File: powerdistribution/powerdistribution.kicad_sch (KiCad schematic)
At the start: 110 parts, among them IC1 STEF01FTR, IC2 STEF01FTR, IC3 STEF01FTR, J1 282837-2, J2 282837-2, J3 M20-6102045, J4 Screw_Terminal_01x02, J5 Screw_Terminal_01x02, Q1 IRLML0030, Q2 IRLML0030, Q3 MMBT3904, Q4 SI4925DDY-T1-GE3, SW1 RA1H1C112R, SW2 RA1H1C112R, U1 BQ7790512PW, U2 AP64501QSP-13, U3 AP64501QSP-13, U4 AP64501QSP-13

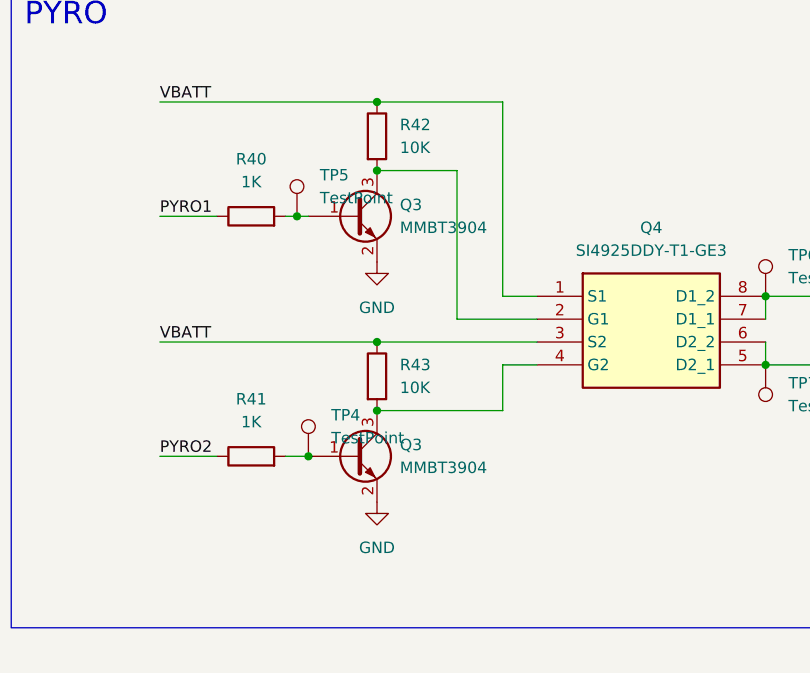
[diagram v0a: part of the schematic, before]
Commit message: swapped pyro transistors for same ones on bms
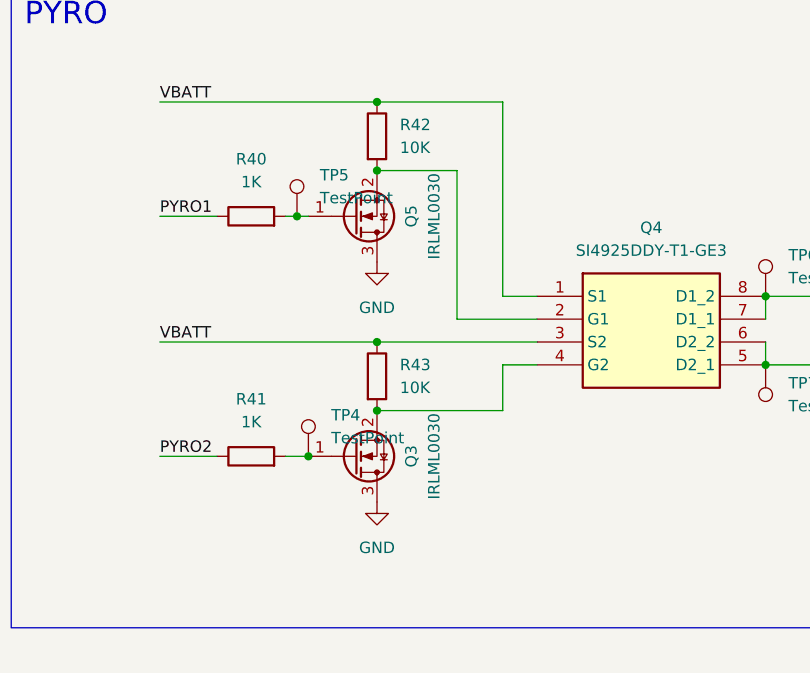
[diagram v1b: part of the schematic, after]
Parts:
- removed Q3 (x2): MMBT3904, Package_TO_SOT_SMD:SOT-23, symbol Transistor_BJT:MMBT3904
- added Q3, Q5: IRLML0030, Package_TO_SOT_SMD:SOT-23, symbol Transistor_FET:IRLML0030
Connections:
- net GND: now also Q3.3 (D), Q5.3 (D)
- net at R41.2, TP4.1: now also Q3.1 (G)
- net at Q4.2 (G1), R42.2: now also Q5.2 (S)
- net at Q4.4 (G2), R43.2: now also Q3.2 (S)
- net at R40.2, TP5.1: now also Q5.1 (G)
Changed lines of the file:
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@@
 	)
 	(junction
-		(at 308.61 90.17)
-		(diameter 0)
-		(color 0 0 0 0)
-	)
-	(junction
 		(at 307.34 63.5)
 		(diameter 0)
@@
 	)
 	(junction
-		(at 316.23 85.09)
+		(at 359.41 72.39)
 		(diameter 0)
 		(color 0 0 0 0)
 	)
 	(junction
-		(at 359.41 72.39)
+		(at 367.03 154.94)
 		(diameter 0)
 		(color 0 0 0 0)
 	)
 	(junction
-		(at 367.03 154.94)
+		(at 58.42 72.39)
 		(diameter 0)
 		(color 0 0 0 0)
 	)
 	(junction
-		(at 58.42 72.39)
+		(at 316.23 85.09)
 		(diameter 0)
 		(color 0 0 0 0)
@@
 	)
 	(junction
-		(at 152.4 72.39)
+		(at 316.23 58.42)
 		(diameter 0)
 		(color 0 0 0 0)
 	)
 	(junction
-		(at 173.99 171.45)
+		(at 152.4 72.39)
 		(diameter 0)
 		(color 0 0 0 0)
 	)
 	(junction
-		(at 176.53 246.38)
+		(at 173.99 171.45)
 		(diameter 0)
 		(color 0 0 0 0)
 	)
 	(junction
-		(at 71.12 328.93)
+		(at 176.53 246.38)
 		(diameter 0)
 		(color 0 0 0 0)
 	)
 	(junction
-		(at 316.23 58.42)
+		(at 71.12 328.93)
 		(diameter 0)
 		(color 0 0 0 0)
@@
 	)
 	(junction
+		(at 308.61 90.17)
+		(diameter 0)
+		(color 0 0 0 0)
+	)
+	(junction
 		(at 83.82 323.85)
 		(diameter 0)
@@
 	)
 	(symbol
+		(lib_id "Transistor_FET:IRLML0030")
+		(at 313.69 63.5 0)
+		(mirror x)
+		(unit 1)
+		(exclude_from_sim no)
+		(in_bom yes)
+		(on_board yes)
+		(dnp no)
+		(property "Reference" "Q5"
+			(at 320.04 63.5 90)
+			(effects
+				(font
+					(size 1.27 1.27)
+				)
+			)
+		)
+		(property "Value" "IRLML0030"
+			(at 322.58 63.5 90)
+			(effects
+				(font
+					(size 1.27 1.27)
+				)
+			)
+		)
+		(property "Footprint" "Package_TO_SOT_SMD:SOT-23"
+			(at 318.77 61.595 0)
+			(effects
+				(font
+					(size 1.27 1.27)
+					(italic yes)
+				)
+				(justify left)
+				(hide yes)
+			)
+		)
+		(property "Datasheet" "https://www.infineon.com/dgdl/irlml0030pbf.pdf?fileId=5546d462533600a401535664773825df"
+			(at 318.77 59.69 0)
+			(effects
+				(font
+					(size 1.27 1.27)
+				)
+				(justify left)
+				(hide yes)
+			)
+		)
+		(property "Description" "5.3A Id, 30V Vds, 27mOhm Rds, N-Channel HEXFET Power MOSFET, SOT-23"
+			(at 313.69 63.5 0)
+			(effects
+				(font
+					(size 1.27 1.27)
+				)
+				(hide yes)
+			)
+		)
+		(pin "2"
+		)
+		(pin "3"
+		)
+		(pin "1"
+		)
+		(instances
+			(project "powerdistribution"
+				(path "/4cf67788-0fe7-4c87-8363-3433eaa0df90"
+					(reference "Q5")
+					(unit 1)
+				)
+			)
+		)
+	)
+	(symbol
 		(lib_id "power:GND")
 		(at 80.01 68.58 0)
@@
 	)
 	(symbol
+		(lib_id "Transistor_FET:IRLML0030")
+		(at 313.69 90.17 0)
+		(mirror x)
+		(unit 1)
+		(exclude_from_sim no)
+		(in_bom yes)
+		(on_board yes)
+		(dnp no)
+		(property "Reference" "Q3"
+			(at 320.04 90.17 90)
+			(effects
+				(font
+					(size 1.27 1.27)
+				)
+			)
+		)
+		(property "Value" "IRLML0030"
+			(at 322.58 90.17 90)
+			(effects
+				(font
+					(size 1.27 1.27)
+				)
+			)
+		)
+		(property "Footprint" "Package_TO_SOT_SMD:SOT-23"
+			(at 318.77 88.265 0)
+			(effects
+				(font
+					(size 1.27 1.27)
+					(italic yes)
+				)
+				(justify left)
+				(hide yes)
+			)
+		)
+		(property "Datasheet" "https://www.infineon.com/dgdl/irlml0030pbf.pdf?fileId=5546d462533600a401535664773825df"
+			(at 318.77 86.36 0)
+			(effects
+				(font
+					(size 1.27 1.27)
+				)
+				(justify left)
+				(hide yes)
+			)
+		)
+		(property "Description" "5.3A Id, 30V Vds, 27mOhm Rds, N-Channel HEXFET Power MOSFET, SOT-23"
+			(at 313.69 90.17 0)
+			(effects
+				(font
+					(size 1.27 1.27)
+				)
+				(hide yes)
+			)
+		)
+		(pin "2"
+		)
+		(pin "3"
+		)
+		(pin "1"
+		)
+		(instances
+			(project "powerdistribution"
+				(path "/4cf67788-0fe7-4c87-8363-3433eaa0df90"
+					(reference "Q3")
+					(unit 1)
+				)
+			)
+		)
+	)
+	(symbol
 		(lib_id "Device:C")
 		(at 367.03 328.93 0)
@@
 	)
 	(symbol
-		(lib_id "Transistor_BJT:MMBT3904")
-		(at 313.69 63.5 0)
-		(unit 1)
-		(exclude_from_sim no)
-		(in_bom yes)
-		(on_board yes)
-		(dnp no)
-		(fields_autoplaced yes)
-		(property "Reference" "Q3"
-			(at 318.77 62.2299 0)
-			(effects
-				(font
-					(size 1.27 1.27)
-				)
-				(justify left)
-			)
-		)
-		(property "Value" "MMBT3904"
-			(at 318.77 64.7699 0)
-			(effects
-				(font
-					(size 1.27 1.27)
-				)
-				(justify left)
-			)
-		)
-		(property "Footprint" "Package_TO_SOT_SMD:SOT-23"
-			(at 318.77 65.405 0)
-			(effects
-				(font
-					(size 1.27 1.27)
-					(italic yes)
-				)
-				(justify left)
-				(hide yes)
-			)
-		)
-		(property "Datasheet" "https://www.onsemi.com/pdf/datasheet/pzt3904-d.pdf"
-			(at 313.69 63.5 0)
-			(effects
-				(font
-					(size 1.27 1.27)
-				)
-				(justify left)
-				(hide yes)
-			)
-		)
-		(property "Description" "0.2A Ic, 40V Vce, Small Signal NPN Transistor, SOT-23"
-			(at 313.69 63.5 0)
-			(effects
-				(font
-					(size 1.27 1.27)
-				)
-				(hide yes)
-			)
-		)
-		(property "MPN" "MMBT3904LT3G"
-			(at 313.69 63.5 0)
-			(effects
-				(font
-					(size 1.27 1.27)
-				)
-				(hide yes)
-			)
-		)
-		(property "Package" "SOT-23-3 (TO-236)"
-			(at 313.69 63.5 0)
-			(effects
-				(font
-					(size 1.27 1.27)
-				)
-				(hide yes)
-			)
-		)
-		(pin "2"
-		)
-		(pin "1"
-		)
-		(pin "3"
-		)
-		(instances
-			(project "powerdistribution"
-				(path "/4cf67788-0fe7-4c87-8363-3433eaa0df90"
-					(reference "Q3")
-					(unit 1)
-				)
-			)
-		)
-	)
-	(symbol
 		(lib_id "Device:R")
 		(at 302.26 63.5 90)
@@
 					(unit 1)
 				)
-			)
-		)
-	)
-	(symbol
-		(lib_id "Transistor_BJT:MMBT3904")
-		(at 313.69 90.17 0)
-		(unit 1)
-		(exclude_from_sim no)
-		(in_bom yes)
-		(on_board yes)
-		(dnp no)
-		(fields_autoplaced yes)
-		(property "Reference" "Q3"
-			(at 318.77 88.8999 0)
-			(effects
-				(font
-					(size 1.27 1.27)
-				)
-				(justify left)
-			)
-		)
-		(property "Value" "MMBT3904"
-			(at 318.77 91.4399 0)
-			(effects
-				(font
-					(size 1.27 1.27)
-				)
-				(justify left)
-			)
-		)
-		(property "Footprint" "Package_TO_SOT_SMD:SOT-23"
-			(at 318.77 92.075 0)
-			(effects
-				(font
-					(size 1.27 1.27)
-					(italic yes)
-				)
-				(justify left)
-				(hide yes)
-			)
-		)
-		(property "Datasheet" "https://www.onsemi.com/pdf/datasheet/pzt3904-d.pdf"
-			(at 313.69 90.17 0)
-			(effects
-				(font
-					(size 1.27 1.27)
-				)
-				(justify left)
-				(hide yes)
-			)
-		)
-		(property "Description" "0.2A Ic, 40V Vce, Small Signal NPN Transistor, SOT-23"
-			(at 313.69 90.17 0)
-			(effects
-				(font
-					(size 1.27 1.27)
-				)
-				(hide yes)
-			)
-		)
-		(pin "1"
-		)
-		(pin "2"
-		)
-		(pin "3"
-		)
-		(instances
-			(project "powerdistribution"
-				(path "/4cf67788-0fe7-4c87-8363-3433eaa0df90"
-					(reference "Q3")
-					(unit 1)
-				)

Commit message: add models
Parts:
- removed C1, C2, C3, C4: JMK105BJ105KV-F, HPRfootprints:CAPC1005X55N, symbol HPRsymbols:JMK105BJ105KV-F
- removed C5, C6: C, symbol Device:C
- removed R15, R17, R18, R7, R8: R_US, symbol Device:R_US
- added C1, C2, C3, C4: C0603C104K5RACTU, C0603C104K5RACTU:CAPC1608X90, symbol HPRsymbols:C0603C104K5RACTU
- added C37, C38: UMK107AB7105KA-T, UMK107AB7105KA-T:CAPC1608X95N, symbol HPRsymbols:UMK107AB7105KA-T
- added R15, R17: ERJ2RKF1004X, ERJ2RKF1004X:RES_ERJ2RKF1004X, symbol HPRsymbols:ERJ2RKF1004X
- added R44: CSNL2512FT1L00, STA_CSNL25121_STP, symbol HPRsymbols:CSNL2512FT1L00
- added R7: RC1206FR-074K53L, RC1206N_YAG, symbol HPRsymbols:RC1206FR-074K53L
- added R8: RC0603FR-0710KL, RC0603FR-0710KL:RESC1607X60N, symbol HPRsymbols:RC0603FR-0710KL
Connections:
- net AVdd: now also C37.1
- net GND: now also C1.2, C2.2, C3.2, C37.2, C38.1, C4.1, R44.1
- net Vdd: now also C38.2
- net sns-: now also R15.1, R44.2
- net at R4.2, U1.3 (VC5), U1.4 (VC4): now also C4.2
- net at Q2.1 (G), R16.1: now also R17.1
- net at RT1.1, U1.15 (TS): now also R8.1
- net at U1.16 (VTB): now also R8.2
- net at U1.13 (CHG): now also R17.2
- net at U1.11 (DSG): now also R7.2
- net at R3.2, U1.5 (VC3): now also C3.1
- net at R2.2, U1.6 (VC2): now also C2.1
- net at R1.2, U1.7 (VC1): now also C1.1
- net at Q1.1 (G): now also R15.2, R7.1
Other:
- moved on the sheet: RT1

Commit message: bms parts
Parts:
- removed C10, C11: 22 uf, symbol Device:C_Small
- removed C10: 22uf, symbol Device:C_Small
- removed C20, C21, C27, C28: 10 uf, symbol Device:C_Small
- added C10, C20, C5, C6: CL31B106KAHNNNE, CL31B106KAHNNNE:CAPC3216X180N, symbol HPRsymbols:CL31B106KAHNNNE
- C1, C2, C3, C4: footprint C0603C104K5RACTU:CAPC1608X90 -> HPRfootprints:CAPC1608X90
- C37, C38: footprint UMK107AB7105KA-T:CAPC1608X95N -> HPRfootprints:CAPC1608X95N
- J3: footprint RHDR40W66P254_2X20_5146X500X1105P -> HPRfootprints:RHDR40W66P254_2X20_5146X500X1105P
- R15, R17: footprint ERJ2RKF1004X:RES_ERJ2RKF1004X -> HPRfootprints:RES_ERJ2RKF1004X
- R44: footprint STA_CSNL25121_STP -> HPRfootprints:STA_CSNL25121_STP
- R7: footprint RC1206N_YAG -> HPRfootprints:RC1206N_YAG
- R8: footprint RC0603FR-0710KL:RESC1607X60N -> HPRfootprints:RESC1607X60N
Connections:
- net GND: now also C10.1, C20.1, C5.1, C6.1
- net Pack+: now also C10.2, C20.2, C5.2, C6.2

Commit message: buck fixes and new components
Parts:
- removed 100nf1, C29, C30, C31, C32, C33, C34: C, symbol Device:C
- removed C10, C20, C5, C6: CL31B106KAHNNNE, CL31B106KAHNNNE:CAPC3216X180N, symbol HPRsymbols:CL31B106KAHNNNE
- removed C11, C25: 2.7nf, symbol Device:C
- removed C12, C19: 10 nf, symbol Device:C_Small
- removed C14: 10 uf, symbol Device:C_Small
- removed C22: 22uf, symbol Device:C_Small
- removed C35, C36: 100nF, symbol Device:C
- removed IC1, IC2, IC3: STEF01FTR, HPRfootprints:SOP65P640X120-15N, symbol HPRsymbols:STEF01FTR
- removed J4, J5: Screw_Terminal_01x02, symbol Connector:Screw_Terminal_01x02
- removed R10, R11, R12, R13, R14, R28, R29, R30, R31, R32, R33, R34, R35, R36, R37, R38, R39, R9: R, symbol Device:R
- removed R21, R27: 15.8k, symbol Device:R_US
- removed R22, R25: 10k, symbol Device:R_US
- removed R23: 31.6k, symbol Device:R_US
- removed R24: 10.5k, symbol Device:R_US
- removed R26: 52.3, symbol Device:R_US
- removed SW1, SW2: RA1H1C112R, SW_RA1H1C112R_EWI, symbol HPRsymbols:RA1H1C112R
- removed U2, U3, U4: AP64501QSP-13, SO-8EP_DIO, symbol 2025-11-16_06-05-29:AP64501QSP-13
- added C10, C20, C21: 22 uf, symbol Device:C_Small
- added C11: 10 nf, symbol Device:C_Small
- added C12: 100nF, symbol Device:C
- added C14, C22: 2.7nf, symbol Device:C
- added C19: 33pf, symbol Device:C
- added C25: 22uf, symbol Device:C_Small
- added C27, C28, C29, C30, C31: 10uf, symbol Device:C_Small
- added C5: 56pf, symbol Device:C
- added C6: 10nf, symbol Device:C_Small
- added R10: 65k, symbol Device:R_US
- added R11, R14: 10k, symbol Device:R_US
- added R12, R18, R9: 10.5k, symbol Device:R_US
- added R13: 31.6k, symbol Device:R_US
- added U2, U3, U4: AP64501QSP-13, HPRlibrary:SO-8EP_DIO-L, symbol HPRlibrary:AP64501QSP-13
- added U5, U6: TPS1HC30BQPWPRQ1, HPRlibrary:IC_TPS1HC30BQPWPRQ1, symbol HPRlibrary:TPS1HC30BQPWPRQ1
- C13: value 10 uf -> 22uf
- C15: value 22uf -> 22 uf
- C16: value 22 uf -> 22uf
- C17: value 22 uf -> 10 nf
- C18: value 2.7nf -> 100nF
- C26: value 10 nf -> 10uf
- C7: value C -> 100nF
- C8: value C -> 33pf; now not fitted
- C9: value C -> 2.7nf
- L2: value 4.7uh -> 6.8 uh
- R19: value 10k -> 52.3k
- R20: value 52.3 -> 10k
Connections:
- net GND: now also C15.2, C16.2, C17.1, C23.2, C24.2, R20.1, C10.2, C11.1, C14.2, C19.2, C20.2, C21.2, C22.2, C25.2, C27.1, C28.1, C29.1, C30.1, C31.1, C5.2, C6.1, R11.1, R14.1, U2.7 (GND), U2.EPAD (EXPOSED_PAD), U3.7 (GND), U3.EPAD (EXPOSED_PAD), U4.7 (GND), U4.EPAD (EXPOSED_PAD); no longer C7.1, R19.1
- net Pack+: now also C26.2, C27.2, C28.2, C29.2, C30.2, C31.2, U2.2 (VIN), U2.3 (EN), U3.2 (VIN), U3.3 (EN), U4.2 (VIN), U4.3 (EN); no longer C13.1
- net at C7.2: now also L1.2, U2.8 (SW)
- net 6V: now reaches L1.1
- net 6V: now also C15.1, C16.1, C10.1, R10.1
- net 3.3V: now reaches L2.1
- net 3.3V: now also C13.1, C20.1, C21.1, R13.1
- net 5V: now reaches L3.1
- net 5V: now also C23.1, C24.1, R19.1, C25.1
- net at R19.2: now also R20.2, U3.5 (FB); no longer R20.1
- net at C18.1: now also U3.1 (BST)
- net 3.3v_output: no longer names the net of L2.2
- net 3.3v_output: now also C12.2, U4.8 (SW)
- removed net 5v_output: C23.2, C24.2, L1.2
- removed net 6v_output: C15.2, C16.2, C17.2, L3.2, R20.2
- removed net GNDREF: C15.1, C16.1, C17.1, C18.2, C23.1, C24.1
- net Vin_efuse: no longer names the net of C8.1
- net Vin_efuse: now also R9.1, U2.6 (COMP)
- net Vout_efuse: no longer names the net of C9.1
- net Vout_efuse: now also R9.2
- new net: C14.1, R12.2
- new net: C19.1, R18.1, U3.6 (COMP)
- new net: C12.1, U4.1 (BST)
- new net: R13.2, R14.2, U4.5 (FB)
- new net: C5.1, R12.1, U4.6 (COMP)
- new net: R10.2, R11.2, U2.5 (FB)
- new net: C11.2, U4.4 (SS)
- new net: C22.1, R18.2
- new net: C6.2, U2.4 (SS)
- new net: C18.2, L3.2, U3.8 (SW)
- new net: C7.1, U2.1 (BST)
- new net: C17.2, U3.4 (SS)
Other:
- note removed: "E-Fuse"
- note removed: "E-Fuse [DNP]"
- moved on the sheet: J3

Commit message: high side switch
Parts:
- removed C12, C18: 100nF, symbol Device:C
- removed C13, C25: 22uf, symbol Device:C_Small
- removed C17: 10 nf, symbol Device:C_Small
- removed C19: 33pf, symbol Device:C
- removed C22: 2.7nf, symbol Device:C
- removed C24: 22 uf, symbol Device:C_Small
- removed C28: 10uf, symbol Device:C_Small
- removed C5: 56pf, symbol Device:C
- removed Q4: SI4925DDY-T1-GE3, HPRfootprints:SOIC127P600X175-8N, symbol HPRsymbols:SI4925DDY-T1-GE3
- removed TP4, TP5, TP6, TP7: TestPoint, TestPoint:TestPoint_Pad_1.0x1.0mm, symbol Connector:TestPoint
- added C12: 10nf, Capacitor_SMD:C_0603_1608Metric_Pad1.08x0.95mm_HandSolder, symbol Device:C_Small
- added C13, C24: 100nF, Capacitor_SMD:C_0603_1608Metric_Pad1.08x0.95mm_HandSolder, symbol Device:C
- added C17, C28: 2.7nf, Capacitor_SMD:C_0603_1608Metric_Pad1.08x0.95mm_HandSolder, symbol Device:C
- added C18, C19: 22 uf, Capacitor_SMD:C_0603_1608Metric_Pad1.08x0.95mm_HandSolder, symbol Device:C_Small
- added C22, C5: 10uf, Capacitor_SMD:C_0603_1608Metric_Pad1.08x0.95mm_HandSolder, symbol Device:C_Small
- added C25: 33pf, Capacitor_SMD:C_0603_1608Metric_Pad1.08x0.95mm_HandSolder, symbol Device:C
- added C32, C33, C34, C35: 220nf, Capacitor_SMD:C_0603_1608Metric_Pad1.08x0.95mm_HandSolder, symbol Device:C_Small
- added R21, R22, R24, R25, R26, R28, R29, R30, R32, R34: 5k, Resistor_SMD:R_0603_1608Metric_Pad0.98x0.95mm_HandSolder, symbol Device:R_US
- added R23, R31: ~, Resistor_SMD:R_0603_1608Metric_Pad0.98x0.95mm_HandSolder, symbol Device:R_US
- added R27, R33: 1k, Resistor_SMD:R_0603_1608Metric_Pad0.98x0.95mm_HandSolder, symbol Device:R_US
- added R35, R36: 10k, Resistor_SMD:R_0603_1608Metric_Pad0.98x0.95mm_HandSolder, symbol Device:R
- added TP1, TP2: TestPoint, Connector_PinHeader_2.00mm:PinHeader_1x01_P2.00mm_Vertical, symbol Connector:TestPoint
- added U7: ESP32-DEVKIT-V1, HPRlibrary:MODULE_ESP32_DEVKIT_V1, symbol HPRlibrary:ESP32-DEVKIT-V1
- C10, C15, C16, C26, C27, C6, C7, C8, C9: footprint (none) -> Capacitor_SMD:C_0603_1608Metric_Pad1.08x0.95mm_HandSolder
- C11: value 10 nf -> 10uf; footprint (none) -> Capacitor_SMD:C_0603_1608Metric_Pad1.08x0.95mm_HandSolder
- C14: value 2.7nf -> 33pf; footprint (none) -> Capacitor_SMD:C_0603_1608Metric_Pad1.08x0.95mm_HandSolder
- C20: value 22 uf -> 22uf; footprint (none) -> Capacitor_SMD:C_0603_1608Metric_Pad1.08x0.95mm_HandSolder
- C21: value 22 uf -> 10uf; footprint (none) -> Capacitor_SMD:C_0603_1608Metric_Pad1.08x0.95mm_HandSolder; now fitted
- C23: value 22 uf -> 10nf; footprint (none) -> Capacitor_SMD:C_0603_1608Metric_Pad1.08x0.95mm_HandSolder
- C29, C30: value 10uf -> 22 uf; footprint (none) -> Capacitor_SMD:C_0603_1608Metric_Pad1.08x0.95mm_HandSolder
- C31: value 10uf -> 22uf; footprint (none) -> Capacitor_SMD:C_0603_1608Metric_Pad1.08x0.95mm_HandSolder
- R10, R11, R12, R14, R18, R20, R9: footprint (none) -> Resistor_SMD:R_0603_1608Metric_Pad0.98x0.95mm_HandSolder
- R13: value 31.6k -> 65k; footprint (none) -> Resistor_SMD:R_0603_1608Metric_Pad0.98x0.95mm_HandSolder
- R19: value 52.3k -> 65k; footprint (none) -> Resistor_SMD:R_0603_1608Metric_Pad0.98x0.95mm_HandSolder
- R40, R41: value 1K -> 10k
- U3: now not fitted
- U4: now fitted
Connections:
- net 6V: now also C20.1, C29.1, C30.1, C31.1, L2.1, L3.1, R13.1, R19.1, C18.1, C19.1
- net GND: now also C21.1, C23.1, C29.2, C30.2, C31.2, R42.2, R43.2, U5.1 (GND), U5.15 (EXP), U6.1 (GND), U6.15 (EXP), C12.1, C17.2, C18.2, C19.2, C22.1, C25.2, C28.2, C32.1, C33.1, C34.1, C35.1, C5.1, R22.1, R23.2, R27.1, R30.1, R31.2, R33.1, R35.1, R36.1; no longer C21.2, C23.2, C29.1, C30.1, C31.1, J1.2, J2.2
- net PYRO1: now also Q5.1 (G), R36.2; no longer R40.1
- net PYRO2: now also Q3.1 (G), R35.2; no longer R41.1
- net Pack+: now also U5.12 (VBB), U5.13 (VBB__1), U6.12 (VBB), U6.13 (VBB__1), C32.2, C34.2; no longer C26.2, C27.2, C29.2, C30.2, C31.2, U2.2 (VIN), U2.3 (EN), U3.2 (VIN), U3.3 (EN), U4.2 (VIN), U4.3 (EN)
- net VBATT: now also J1.1, J2.1; no longer R42.1, R43.1
- net at C14.1: now also R12.1, U3.6 (COMP); no longer R12.2
- net at R41.2: now also J2.2, Q3.2 (S), R43.1; no longer Q3.1 (G)
- net at Q5.2 (S): now also J1.2, R40.2, R42.1; no longer R42.2
- net at R18.1: now also U4.6 (COMP), C25.1; no longer U3.6 (COMP)
- net at U4.1 (BST): now also C24.1
- net at L2.2: now also U3.8 (SW), C13.2; no longer U4.8 (SW)
- net at R13.2, R14.2: now also U3.5 (FB); no longer U4.5 (FB)
- net at U5.10 (VOUT__1): now also C26.2, C27.2, U2.2 (VIN), U2.3 (EN), U5.9 (VOUT)
- net at U5.2 (EN): now also R21.2
- net at U5.3 (DIAG_EN): now also R26.2
- net at U5.4 (~{FAULT}): now also R25.1
- net at U5.5 (LATCH): now also R22.2
- net at U5.6 (SNS): now also R24.1, R27.2
- net at U5.7 (ILIM): now also R23.1
- net at R19.2, R20.2: now also U4.5 (FB); no longer U3.5 (FB)
- net at C11.2: now also U3.2 (VIN), U3.3 (EN), C5.2; no longer U4.4 (SS)
- net at R18.2: now also C28.1
- net at L3.2: now also U4.8 (SW), C24.2; no longer U3.8 (SW)
- net at U3.1 (BST): now also C13.1
- net at U3.4 (SS): now also C12.2
- net at U6.10 (VOUT__1): now also C21.2, U4.2 (VIN), U4.3 (EN), U6.9 (VOUT), C22.2
- net at U6.2 (EN): now also R28.2
- net at U6.3 (DIAG_EN): now also R29.2
- net at U6.4 (~{FAULT}): now also R32.1
- net at U6.5 (LATCH): now also R30.2
- net at U6.6 (SNS): now also R33.2, R34.1
- net at U6.7 (ILIM): now also R31.1
- removed net 3.3V: C20.1, C21.1, L2.1, R13.1
- removed net 5V: C23.1, L3.1, R19.1
- new net: R28.1, TP2.1
- new net: C23.2, U4.4 (SS)
- new net: C17.1, R12.2
- new net: R21.1, TP1.1
- new net: U7.2 (GND), U7.29 (GND)
- new net 5v_cursns: C35.2, R34.2
- new net 5v_fault: R32.2
- new net 6v_cursns: C33.2, R24.2
- new net 6v_fault: R25.2
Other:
- note added: "3.3V LDO"
- note added: "CONNECTOR"
- note added: "ESP32"
- note added: "PIN SWITCH"
- note added: "Switch"
- moved on the sheet: C10, C15, C16, C26, C27, C6, C7, C8, C9, J1, J2, J3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
